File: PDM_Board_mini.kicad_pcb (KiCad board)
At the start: 4 copper layers, 31.2 x 26.5 mm, 17 parts, among them J1 705550003, J2 705550001, U1 FAN3852UC16X

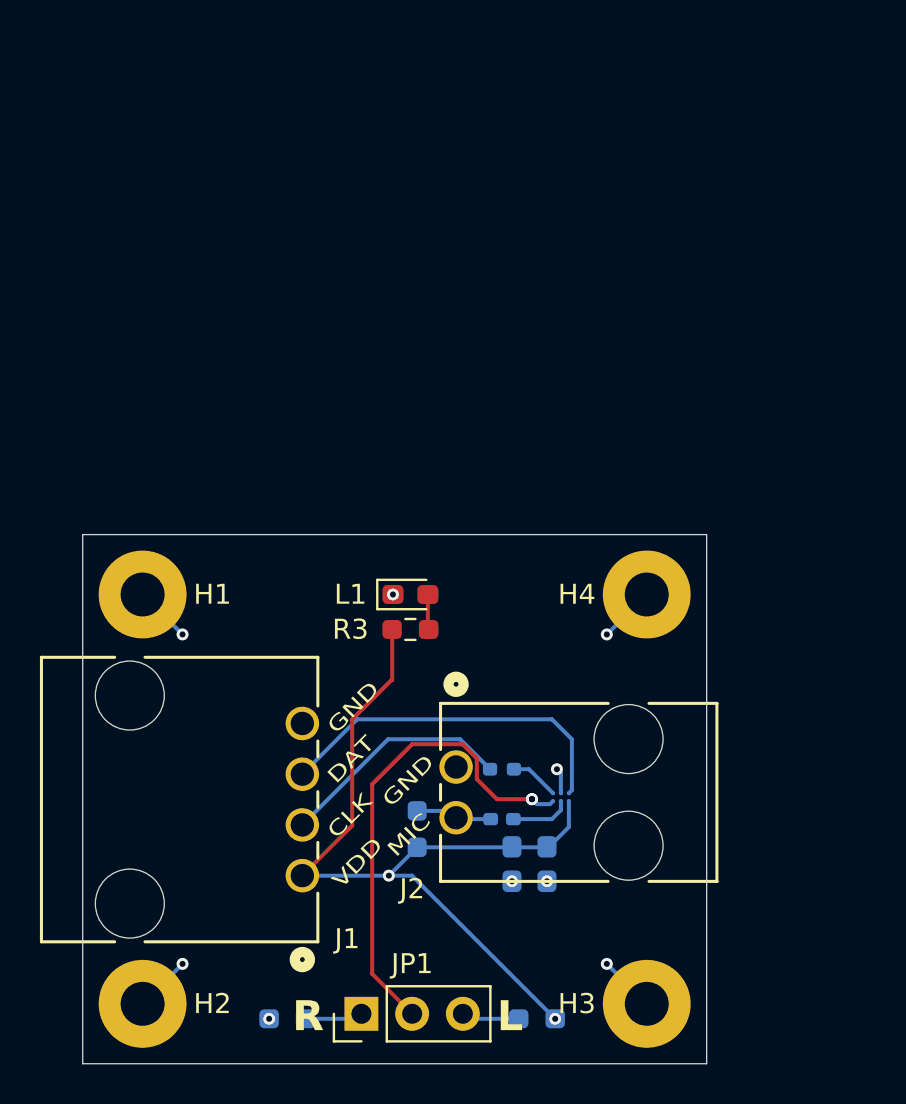
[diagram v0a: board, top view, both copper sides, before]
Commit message: Updated PCB to 2 layer with components on only 1 side
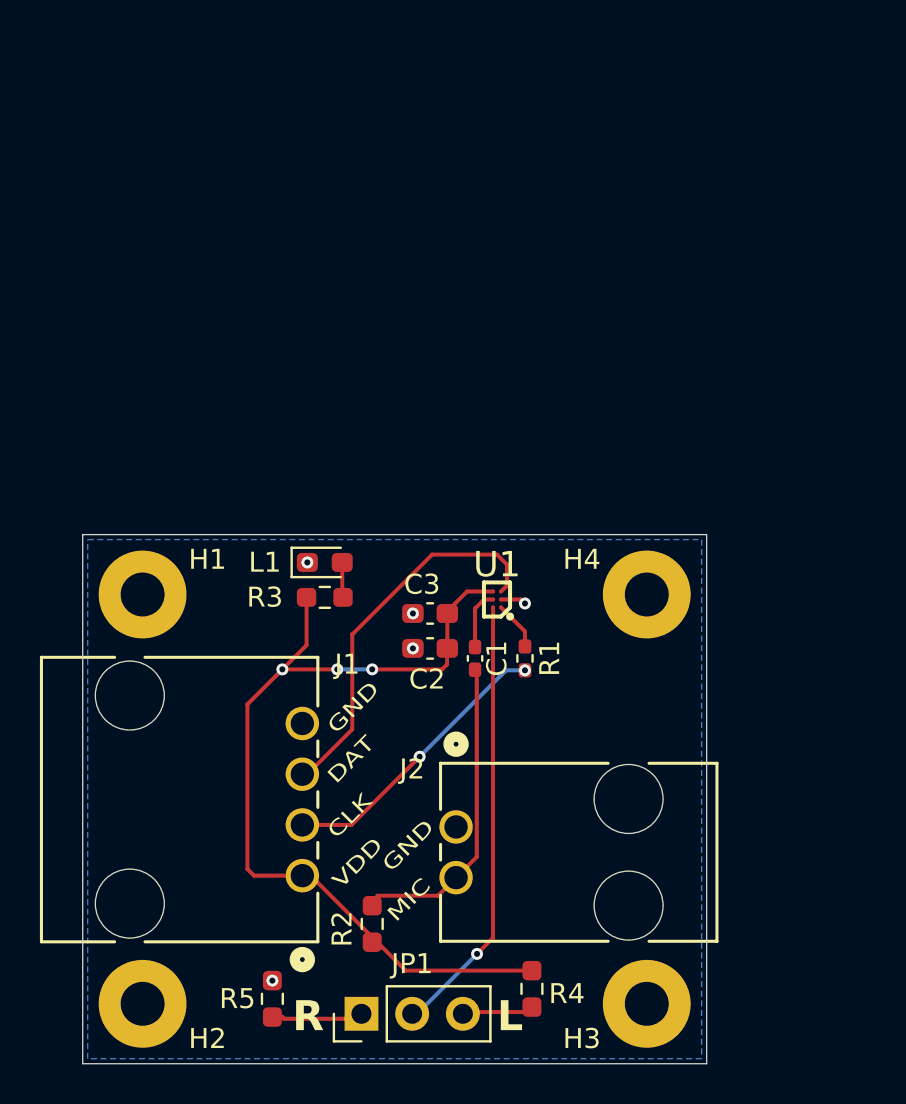
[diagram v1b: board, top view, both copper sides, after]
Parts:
- C1, C2, C3, R1, R2, R4, R5, U1: moved to F.Cu
- moved C3 13.8 mm to (144.4, 115.2), turned to 180 degrees
- moved C2 11.6 mm to (144.4, 117.0), turned to 0 degrees
- moved U1 10.4 mm to (147.8, 114.5), turned to 180 degrees
- moved C1 8.16 mm to (146.7, 117.5), turned to -90 degrees
- moved R1 5.67 mm to (149.2, 117.5), turned to 90 degrees
- moved R2 5.26 mm to (141.5, 130.8)
- moved L1 4.58 mm to (139.1, 112.6)
- moved R3 4.58 mm to (139.1, 114.4)
- moved J2 3.00 mm to (145.7, 125.9)
- moved R4 1.52 mm to (149.5, 134.0), turned to 90 degrees
- moved R5 1.25 mm to (136.5, 134.5), turned to -90 degrees
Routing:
- net IN: track 3.85 -> 15.2 mm
- net GND: track 12.6 -> 1.28 mm, vias 9 -> 5
- net VDD: track 41.1 -> 44.8 mm, vias 2 -> 3
- net CLK: track 11.8 -> 14.4 mm, vias 0 -> 2
- net Net-(JP1-A): track 2.90 -> 5.31 mm
- net J_OUT: track 24.0 -> 22.2 mm, vias 2 -> 1
- net DAT: track 17.8 -> 19.3 mm
- net Net-(JP1-B): track 2.90 -> 3.75 mm
- added copper zone on B.Cu, net GND
- removed copper zone on In2.Cu, net GND
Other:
- copper layers 4 -> 2

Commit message: Added new gerber and image for 2 side pcb
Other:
- board text added: "Danny C Gene W"
- board text added: "ELECTRET TO PDM"
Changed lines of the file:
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@@
 		(capping no)
 		(filling no)
-		(zone_defaults)
 		(pcbplotparams
 			(layerselection 0x00000000_00000000_55555555_5755f5ff)
@@
 		(tags "capacitor handsolder")
 		(property "Reference" "C1"
-			(at 0 -1.1 90)
+			(at 0.05 -1.1 90)
 			(layer "F.SilkS")
 			(effects
@@
 		(tags "resistor handsolder")
 		(property "Reference" "R1"
-			(at 0 1.25 90)
+			(at -0.05 1.1 90)
 			(layer "F.SilkS")
 			(effects
@@
 		(layer "Edge.Cuts")
 	)
+	(gr_text "Danny C\nGene W"
+		(at 157.25 122 0)
+		(layer "F.SilkS")
+		(effects
+			(font
+				(size 0.4 0.5)
+				(thickness 0.0625)
+			)
+			(justify right bottom)
+		)
+	)
+	(gr_text "ELECTRET\nTO PDM"
+		(at 157.5 120.75 0)
+		(layer "F.SilkS")
+		(effects
+			(font
+				(size 0.75 1)
+			)
+			(justify right bottom)
+		)
+	)
 	(gr_text "GND"
 		(at 139.75 121.33 45)
@@
 	)
 	(segment
+		(start 137 135.4125)
+		(end 136.5 135.4125)
+		(width 0.2)
+		(layer "F.Cu")
+		(net "Net-(JP1-A)")
+	)
+	(segment
+		(start 140.46 135.25)
+		(end 140.71 135.5)
+		(width 0.2)
+		(layer "F.Cu")
+		(net "Net-(JP1-A)")
+	)
+	(segment
+		(start 137.0875 135.5)
+		(end 137 135.4125)
+		(width 0.2)
+		(layer "F.Cu")
+		(net "Net-(JP1-A)")
+	)
+	(segment
+		(start 140.96 135.25)
+		(end 140.71 135.5)
+		(width 0.2)
+		(layer "F.Cu")
+		(net "Net-(JP1-A)")
+	)
+	(segment
+		(start 140.71 135.5)
+		(end 137.0875 135.5)
+		(width 0.2)
+		(layer "F.Cu")
+		(net "Net-(JP1-A)")
+	)
+	(segment
+		(start 140.71 135.5)
+		(end 140.96 135.25)
+		(width 0.2)
+		(layer "B.Cu")
+		(net "Net-(JP1-A)")
+	)
+	(segment
 		(start 140 114.35625)
 		(end 140.0375 114.39375)
@@
 	)
 	(segment
-		(start 137 135.4125)
-		(end 136.5 135.4125)
+		(start 146.65 114.95)
+		(end 147.1 114.5)
 		(width 0.2)
 		(layer "F.Cu")
-		(net "Net-(JP1-A)")
+		(net "Net-(U1-Input)")
 	)
 	(segment
-		(start 140.46 135.25)
-		(end 140.71 135.5)
+		(start 147.1 114.5)
+		(end 147.55 114.5)
 		(width 0.2)
 		(layer "F.Cu")
-		(net "Net-(JP1-A)")
+		(net "Net-(U1-Input)")
 	)
 	(segment
-		(start 137.0875 135.5)
-		(end 137 135.4125)
+		(start 146.65 116.8825)
+		(end 146.65 114.95)
 		(width 0.2)
 		(layer "F.Cu")
-		(net "Net-(JP1-A)")
+		(net "Net-(U1-Input)")
 	)
 	(segment
-		(start 140.96 135.25)
-		(end 140.71 135.5)
+		(start 146.7378 127.3922)
+		(end 145.6996 128.4304)
 		(width 0.2)
 		(layer "F.Cu")
-		(net "Net-(JP1-A)")
+		(net "IN")
 	)
 	(segment
-		(start 140.71 135.5)
-		(end 137.0875 135.5)
+		(start 146.65 118.0175)
+		(end 146.7378 118.1053)
 		(width 0.2)
 		(layer "F.Cu")
-		(net "Net-(JP1-A)")
-	)
-	(segment
-		(start 140.71 135.5)
-		(end 140.96 135.25)
-		(width 0.2)
-		(layer "B.Cu")
-		(net "Net-(JP1-A)")
+		(net "IN")
 	)
 	(segment
-		(start 147.55 131.45)
-		(end 147.55 114.9)
+		(start 144.7925 129.3375)
+		(end 145.6996 128.4304)
 		(width 0.2)
 		(layer "F.Cu")
-		(net "J_OUT")
+		(net "IN")
 	)
 	(segment
-		(start 146.75 132.25)
-		(end 147.55 131.45)
+		(start 146.7378 118.1053)
+		(end 146.7378 127.3922)
 		(width 0.2)
 		(layer "F.Cu")
-		(net "J_OUT")
-	)
-	(via
-		(at 146.75 132.25)
-		(size 0.6)
-		(drill 0.3)
-		(layers "F.Cu" "B.Cu")
-		(net "J_OUT")
-	)
-	(segment
-		(start 143.75 135.25)
-		(end 143.5 135.25)
-		(width 0.2)
-		(layer "B.Cu")
-		(net "J_OUT")
+		(net "IN")
 	)
 	(segment
-		(start 146.75 132.25)
-		(end 143.75 135.25)
+		(start 141.75 129.3375)
+		(end 144.7925 129.3375)
 		(width 0.2)
-		(layer "B.Cu")
-		(net "J_OUT")
+		(layer "F.Cu")
+		(net "IN")
 	)
 	(segment
@@
 	)
 	(segment
-		(start 140.46 125.79)
-		(end 143.875 122.375)
+		(start 147.55 131.45)
+		(end 147.55 114.9)
 		(width 0.2)
 		(layer "F.Cu")
-		(net "CLK")
+		(net "J_OUT")
 	)
 	(segment
-		(start 138 125.79)
-		(end 140.46 125.79)
+		(start 146.75 132.25)
+		(end 147.55 131.45)
 		(width 0.2)
 		(layer "F.Cu")
-		(net "CLK")
-	)
-	(via
-		(at 143.875 122.375)
-		(size 0.6)
-		(drill 0.3)
-		(layers "F.Cu" "B.Cu")
-		(net "CLK")
+		(net "J_OUT")
 	)
 	(via
-		(at 149.15 118.0475)
+		(at 146.75 132.25)
 		(size 0.6)
 		(drill 0.3)
 		(layers "F.Cu" "B.Cu")
-		(net "CLK")
+		(net "J_OUT")
 	)
 	(segment
-		(start 148.2025 118.0475)
-		(end 149.15 118.0475)
+		(start 143.75 135.25)
+		(end 143.5 135.25)
 		(width 0.2)
 		(layer "B.Cu")
-		(net "CLK")
+		(net "J_OUT")
 	)
 	(segment
-		(start 143.875 122.375)
-		(end 148.2025 118.0475)
+		(start 146.75 132.25)
+		(end 143.75 135.25)
 		(width 0.2)
 		(layer "B.Cu")
-		(net "CLK")
+		(net "J_OUT")
+	)
+	(segment
+		(start 147.95 114.9)
+		(end 149.15 116.1)
+		(width 0.2)
+		(layer "F.Cu")
+		(net "Net-(U1-Clock)")
+	)
+	(segment
+		(start 149.15 116.1)
+		(end 149.15 116.8525)
+		(width 0.2)
+		(layer "F.Cu")
+		(net "Net-(U1-Clock)")
 	)
 	(segment
@@
 	)
 	(segment
-		(start 146.7378 127.3922)
-		(end 145.6996 128.4304)
-		(width 0.2)
-		(layer "F.Cu")
-		(net "IN")
-	)
-	(segment
-		(start 146.65 118.0175)
-		(end 146.7378 118.1053)
-		(width 0.2)
-		(layer "F.Cu")
-		(net "IN")
-	)
-	(segment
-		(start 144.7925 129.3375)
-		(end 145.6996 128.4304)
-		(width 0.2)
-		(layer "F.Cu")
-		(net "IN")
-	)
-	(segment
-		(start 146.7378 118.1053)
-		(end 146.7378 127.3922)
-		(width 0.2)
-		(layer "F.Cu")
-		(net "IN")
-	)
-	(segment
-		(start 141.75 129.3375)
-		(end 144.7925 129.3375)
+		(start 140.46 125.79)
+		(end 143.875 122.375)
 		(width 0.2)
 		(layer "F.Cu")
-		(net "IN")
+		(net "CLK")
 	)
 	(segment
-		(start 146.65 114.95)
-		(end 147.1 114.5)
+		(start 138 125.79)
+		(end 140.46 125.79)
 		(width 0.2)
 		(layer "F.Cu")
-		(net "Net-(U1-Input)")
+		(net "CLK")
 	)
-	(segment
-		(start 147.1 114.5)
-		(end 147.55 114.5)
-		(width 0.2)
-		(layer "F.Cu")
-		(net "Net-(U1-Input)")
+	(via
+		(at 143.875 122.375)
+		(size 0.6)
+		(drill 0.3)
+		(layers "F.Cu" "B.Cu")
+		(net "CLK")
 	)
-	(segment
-		(start 146.65 116.8825)
-		(end 146.65 114.95)
-		(width 0.2)
-		(layer "F.Cu")
-		(net "Net-(U1-Input)")
+	(via
+		(at 149.15 118.0475)
+		(size 0.6)
+		(drill 0.3)
+		(layers "F.Cu" "B.Cu")
+		(net "CLK")
 	)
 	(segment
-		(start 147.95 114.9)
-		(end 149.15 116.1)
+		(start 148.2025 118.0475)
+		(end 149.15 118.0475)
 		(width 0.2)
-		(layer "F.Cu")
-		(net "Net-(U1-Clock)")
+		(layer "B.Cu")
+		(net "CLK")
 	)
 	(segment
-		(start 149.15 116.1)
-		(end 149.15 116.8525)
+		(start 143.875 122.375)
+		(end 148.2025 118.0475)
 		(width 0.2)
-		(layer "F.Cu")
-		(net "Net-(U1-Clock)")
+		(layer "B.Cu")
+		(net "CLK")
 	)
 	(zone

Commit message: Redo gerber, drill, and pos with correct offsets
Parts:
- moved J1 25.8 mm to (145.4, 103.6)
- moved C1 25.8 mm to (154.0, 92.7)
- moved C2 25.8 mm to (151.8, 92.2)
- moved C3 25.8 mm to (151.8, 90.5)
- moved H1 25.8 mm to (137.4, 89.5)
- moved H2 25.8 mm to (137.4, 110.0)
- moved H3 25.8 mm to (162.6, 110.0)
- moved H4 25.8 mm to (162.6, 89.5)
- moved J2 25.8 mm to (153.1, 101.1)
- moved JP1 25.8 mm to (148.3, 110.5)
- moved L1 25.8 mm to (146.5, 87.9)
- moved R1 25.8 mm to (156.5, 92.7)
- moved R2 25.8 mm to (148.9, 106.0)
- moved R3 25.8 mm to (146.5, 89.6)
- moved R4 25.8 mm to (156.9, 109.2)
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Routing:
- net VDD: vias 3 -> 2
